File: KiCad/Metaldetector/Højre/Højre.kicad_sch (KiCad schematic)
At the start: 16 parts, among them Q2 NMOS_IRL530, Q4 NMOS_IRL530, Q6 NMOS_IRL530

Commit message: ændret kicad opsætning
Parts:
- added H_Out: Conn_01x01_Pin, symbol Connector:Conn_01x01_Pin
- added R_Load: 47, symbol Device:R
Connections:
- net Højre_out renamed Meas_H_Out
- net Meas_H_Out: now also R_Load.1
- new net: H_Out.1 (Pin_1), R_Load.2
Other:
- moved on the sheet: 5V_pin3, 9V_pin2, C2, D3, D4, GND_pin3, Meas_H1, PWM_1_NOT_In1, PWM_2_In1, Q2, Q4, Q6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

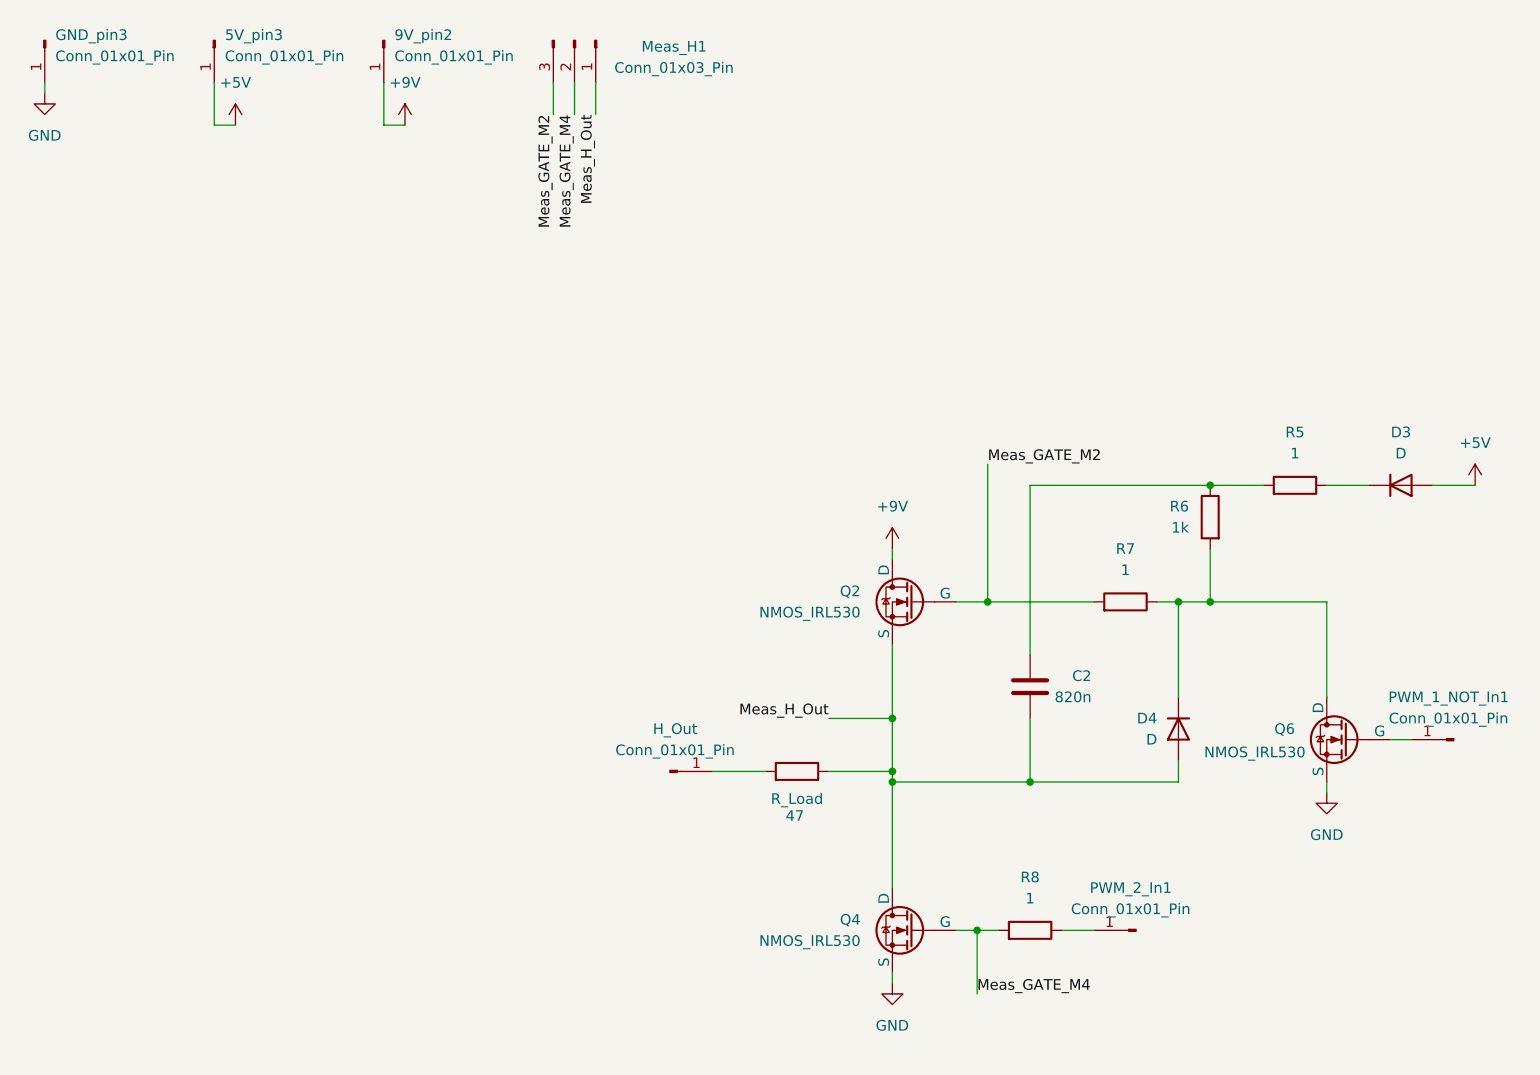
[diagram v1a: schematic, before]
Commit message: nyste pcb design til AP forstærker
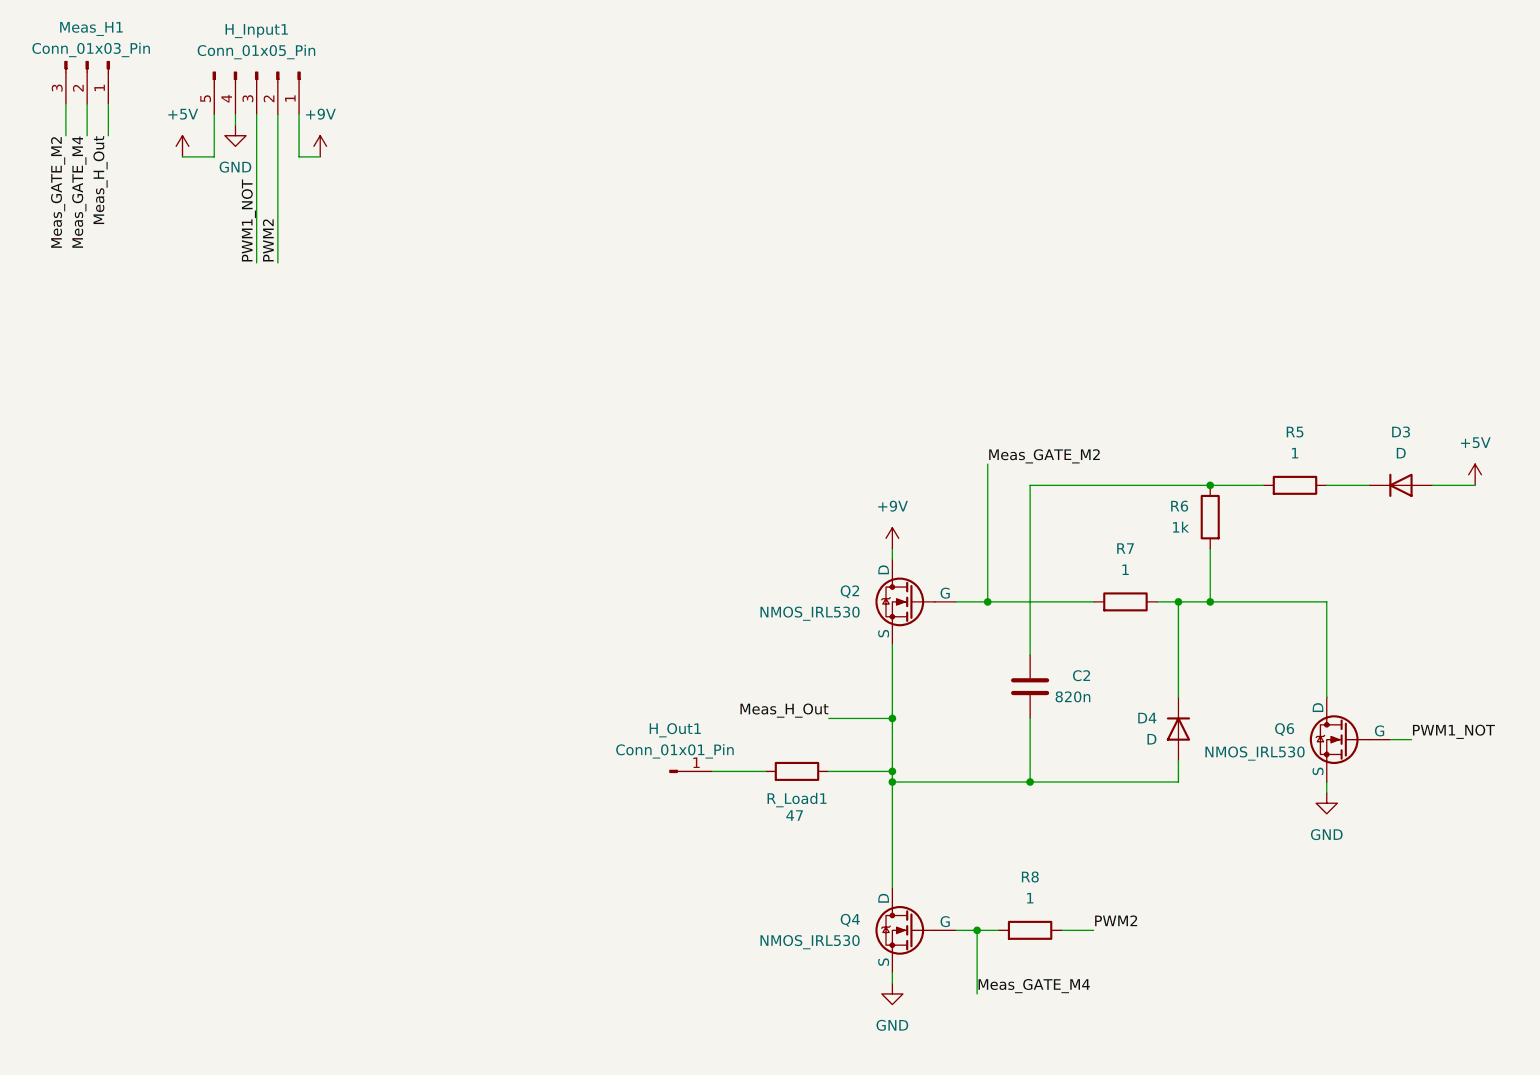
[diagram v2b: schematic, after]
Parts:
- removed 5V_pin3, 9V_pin2, GND_pin3, PWM_1_NOT_In1, PWM_2_In1: Conn_01x01_Pin, symbol Connector:Conn_01x01_Pin
- added H_Input1: Conn_01x05_Pin, Connector_PinHeader_2.54mm:PinHeader_1x05_P2.54mm_Horizontal, symbol Connector:Conn_01x05_Pin
- C2: footprint (none) -> Capacitor_THT:C_Rect_L16.5mm_W8.7mm_P15.00mm_MKT
- D3, D4: footprint (none) -> Diode_THT:D_DO-41_SOD81_P2.54mm_Vertical_AnodeUp
- H_Out1: renamed from H_Out; footprint (none) -> Connector_PinHeader_2.54mm:PinHeader_1x01_P2.54mm_Vertical
- Meas_H1: footprint (none) -> Connector_PinHeader_2.54mm:PinHeader_1x03_P2.54mm_Vertical
- Q2, Q4, Q6: footprint (none) -> Package_TO_SOT_THT:TO-220-3_Vertical
- R5, R6, R7, R8: footprint (none) -> Resistor_THT:R_Axial_DIN0204_L3.6mm_D1.6mm_P5.08mm_Horizontal
- R_Load1: renamed from R_Load; footprint (none) -> Connector_PinHeader_2.54mm:PinHeader_1x02_P2.54mm_Vertical
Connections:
- net +5V: now also H_Input1.5 (Pin_5)
- net +9V: now also H_Input1.1 (Pin_1)
- net GND: now also H_Input1.4 (Pin_4)
- net PWM2: now reaches R8.1
- net PWM2: now also H_Input1.2 (Pin_2)
- net PWM1_NOT: now reaches Q6.2 (G)
- net PWM1_NOT: now also H_Input1.3 (Pin_3)
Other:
- moved on the sheet: Meas_H1
